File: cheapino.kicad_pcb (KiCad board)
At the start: 2 copper layers, 132.5 x 95.1 mm, 52 parts, among them K1 SW_Push, K10 SW_Push, K11 SW_Push, K12 SW_Push, K13 SW_Push, K14 SW_Push, K15 SW_Push, K16 SW_Push, K17 SW_Push, K18 SW_Push, K2 SW_Push, K3 SW_Push, K4 SW_Push, K5 SW_Push, K6 SW_Push, K7 SW_Push, K8 SW_Push, K9 SW_Push, U1 RP2040-Zero

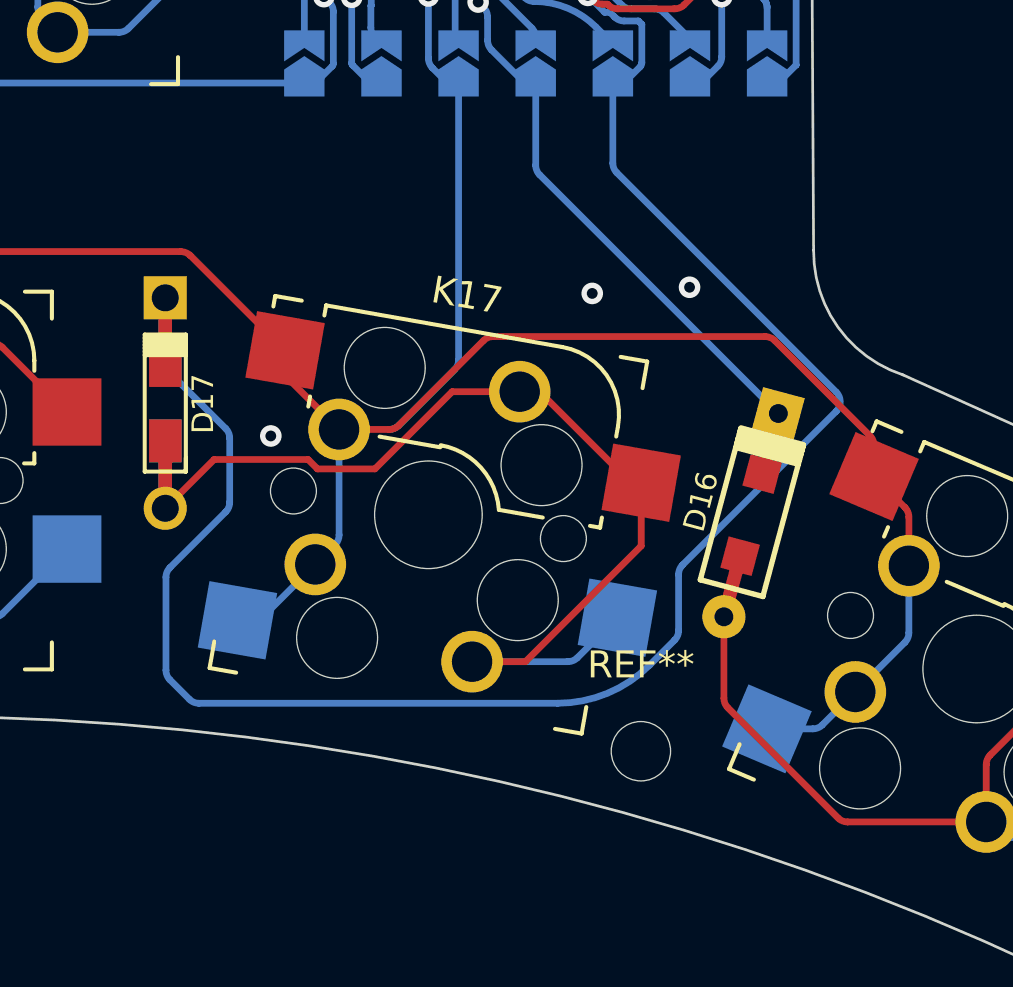
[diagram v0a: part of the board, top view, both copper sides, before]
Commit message: Fix missing SMD footprint on right/back Diodo D16
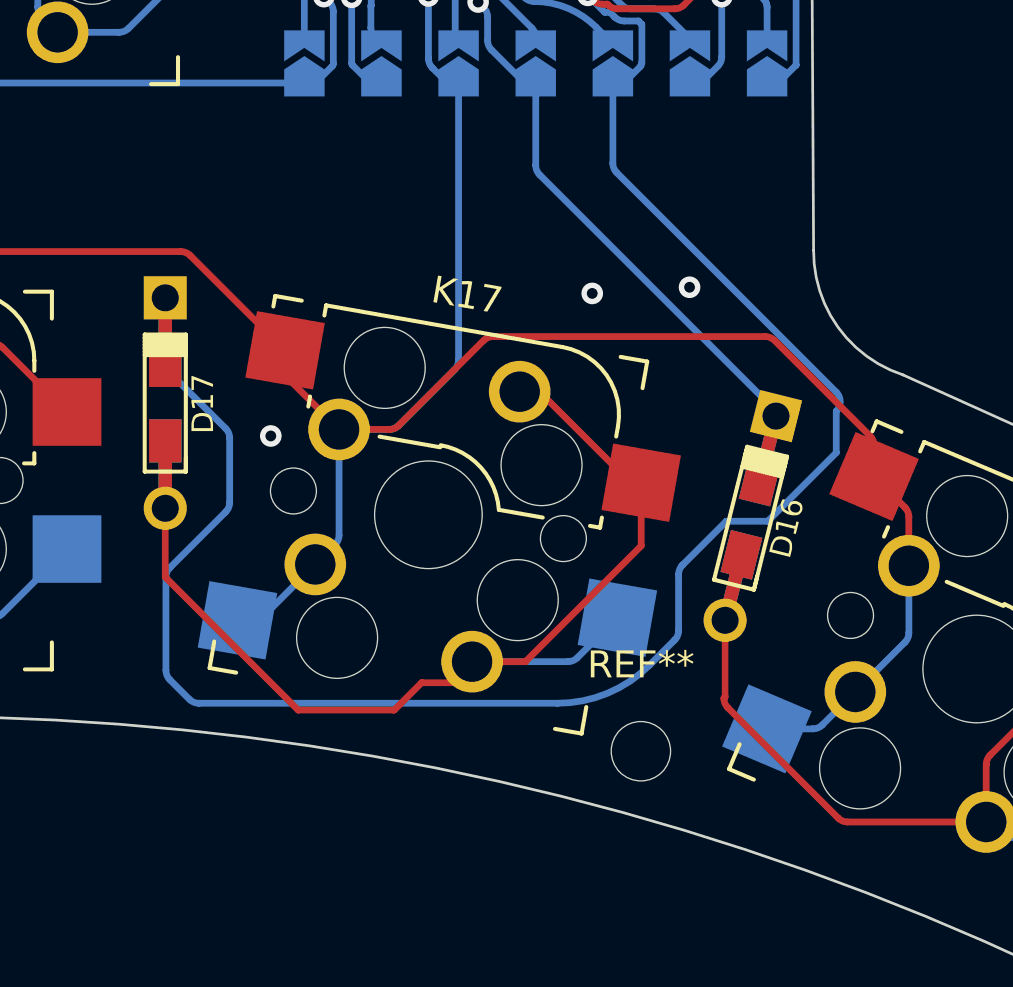
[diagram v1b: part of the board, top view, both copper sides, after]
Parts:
- D16: footprint keyboard_parts:D_SOD123_axial -> keebio:Diode-dual
- moved D16 0.12 mm to (173.2, 124.0), turned to 76 degrees
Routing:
- net Net-(D17-A): track 36.4 -> 37.9 mm
- net ROW_2: track 207.0 -> 207.9 mm

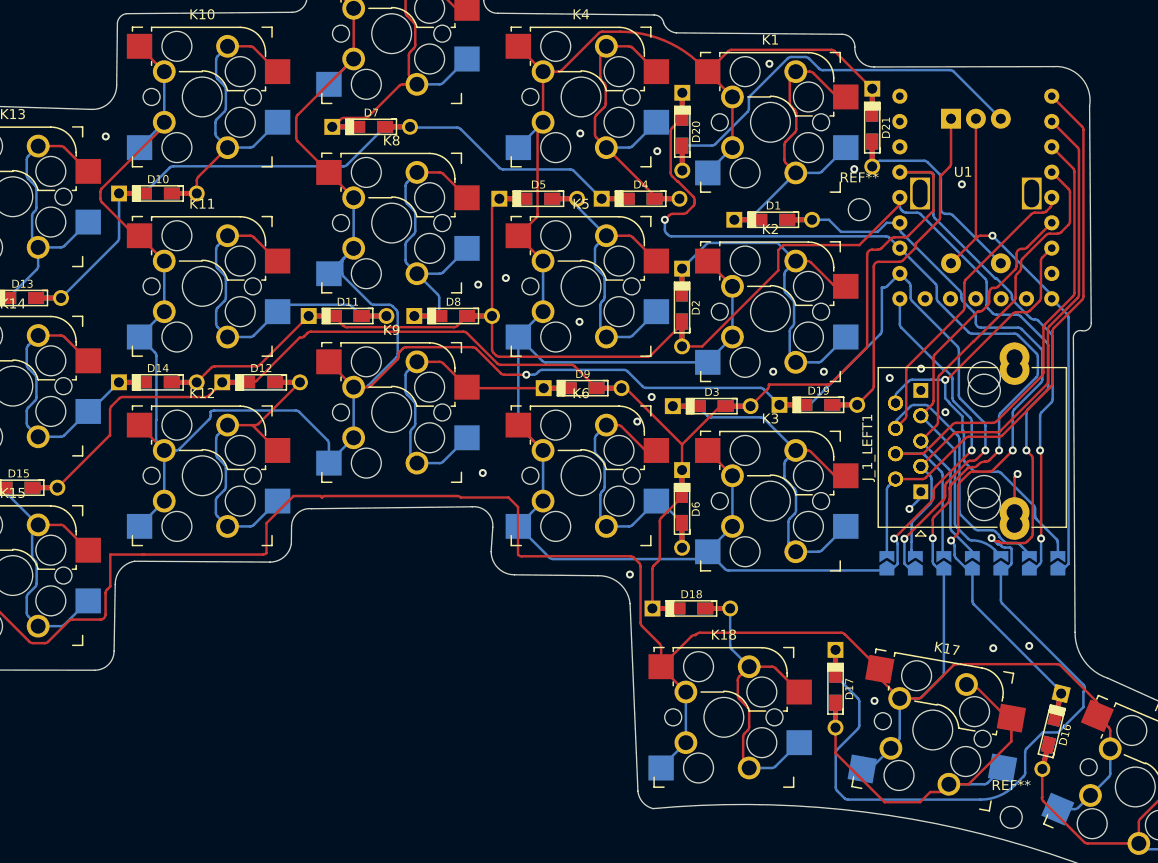
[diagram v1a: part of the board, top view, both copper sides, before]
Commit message: Fixes #10 Added some mounting holes
Also added logo, rounded tracks and tear drops
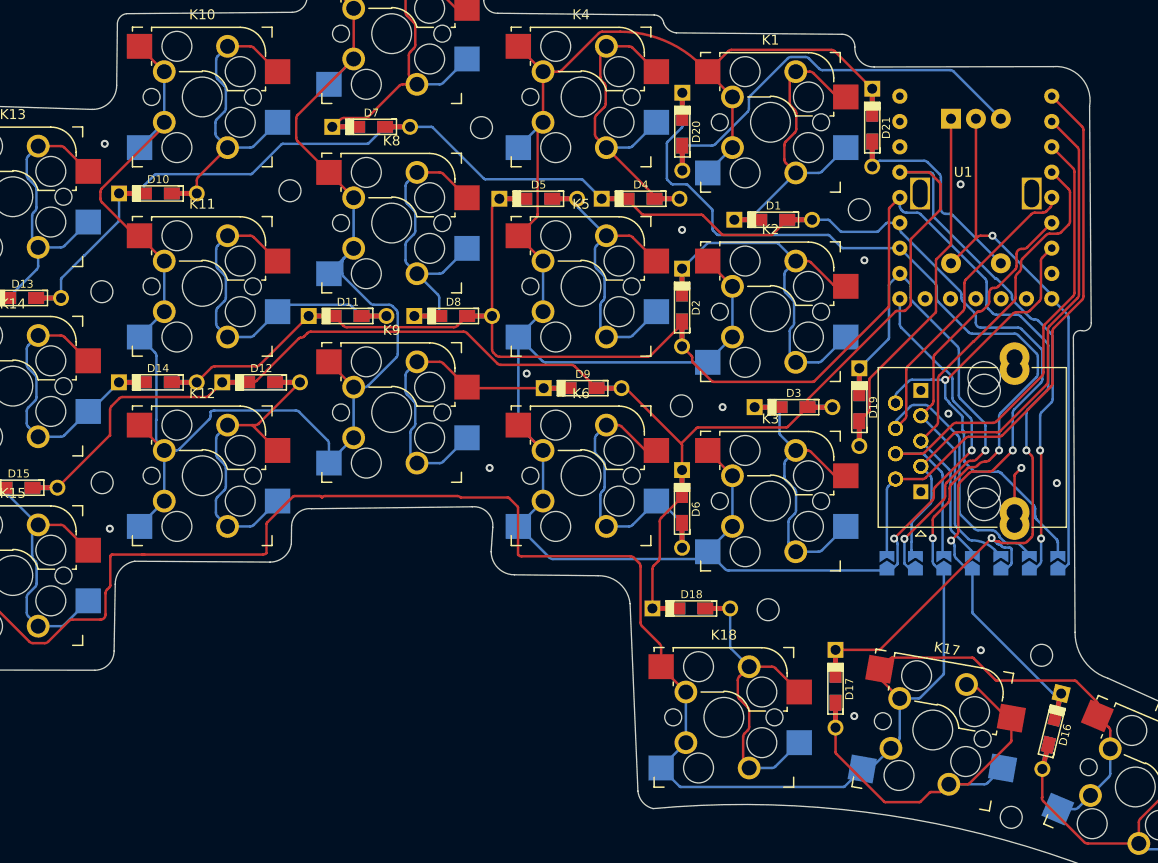
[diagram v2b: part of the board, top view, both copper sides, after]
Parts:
- added REF**: MountingHole_2.2mm_M2, MountingHole:MountingHole_2.2mm_M2, F.Cu at (136.1, 91.3)
- added REF**: MountingHole_2.2mm_M2, MountingHole:MountingHole_2.2mm_M2, F.Cu at (144.8, 111.8)
- added REF**: MountingHole_2.2mm_M2, MountingHole:MountingHole_2.2mm_M2, F.Cu at (78.0, 99.0)
- added REF**: MountingHole_2.2mm_M2, MountingHole:MountingHole_2.2mm_M2, F.Cu at (116.0, 63.4)
- added REF**: MountingHole_2.2mm_M2, MountingHole:MountingHole_2.2mm_M2, F.Cu at (96.8, 69.7)
- added REF**: MountingHole_2.2mm_M2, MountingHole:MountingHole_2.2mm_M2, F.Cu at (77.9, 79.9)
- added REF**: MountingHole_2.2mm_M2, MountingHole:MountingHole_2.2mm_M2, F.Cu at (172.2, 116.3)
- moved D3 8.20 mm to (147.3, 91.4)
- moved D19 4.12 mm to (153.9, 91.4), turned to 90 degrees
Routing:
- net COL_2: track 259.3 -> 205.7 mm, vias 3 -> 2
- net ROW_2: track 207.9 -> 174.8 mm
- net ROW_1: track 138.6 -> 155.4 mm
- net COL_3: track 343.4 -> 336.5 mm, vias 3 -> 2
- net Net-(D3-K): track 35.3 -> 28.7 mm
- net ROW_3: track 178.4 -> 181.0 mm
- net GND: track 8.88 -> 7.26 mm, vias 23 -> 13
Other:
- board text added: "Cheapino 2"
- board text added: "Solder on right side only"
- board text added: "by Tompi"
- board text removed: "Cheapino v2"
- board text removed: "Solder right side only"

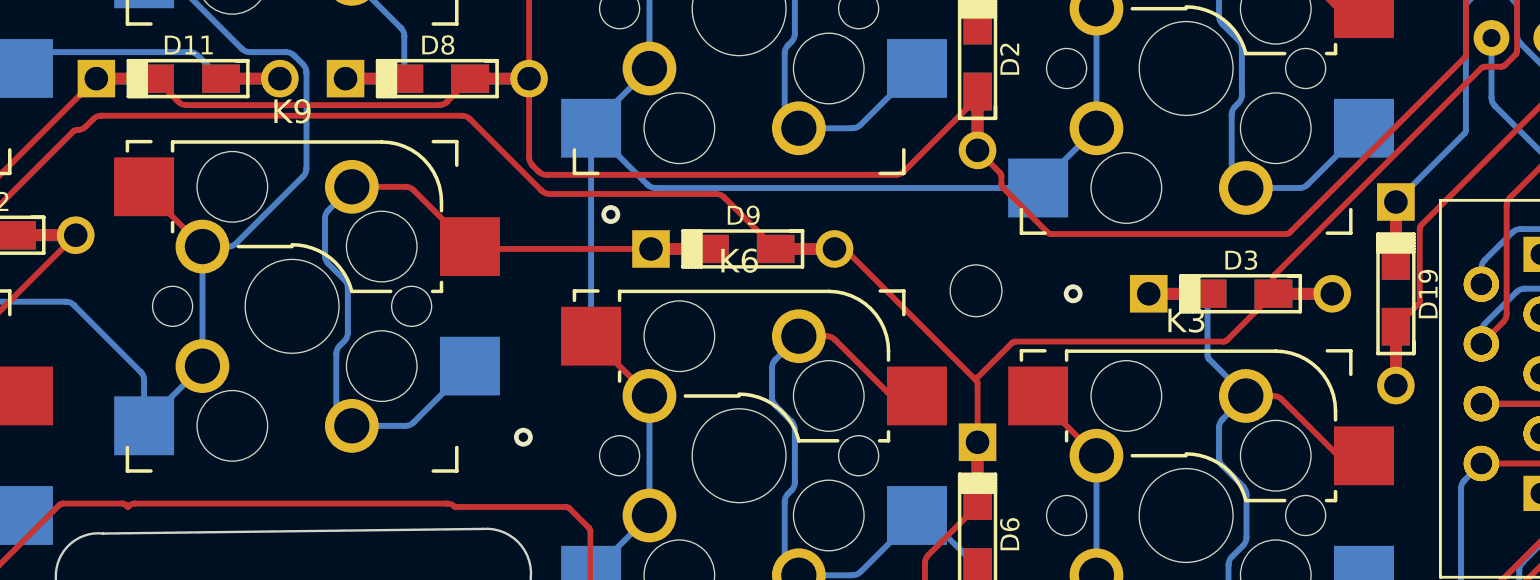
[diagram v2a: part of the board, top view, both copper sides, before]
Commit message: Fix embarassing missing trace for column 2...
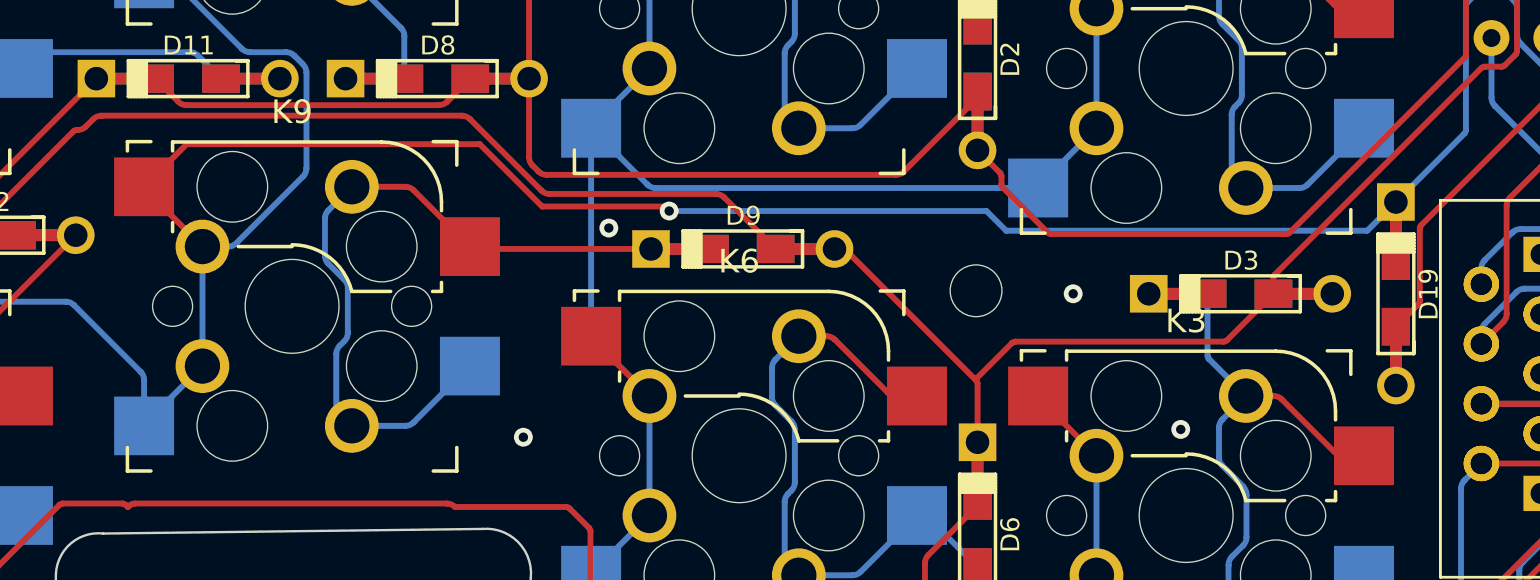
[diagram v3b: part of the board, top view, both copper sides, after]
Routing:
- net COL_2: track 205.7 -> 261.6 mm, vias 2 -> 3
- net GND: vias 13 -> 14
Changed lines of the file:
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@@
   (gr_text "Cheapino 2" (at 174.001658 114.960259) (layer "B.Paste")
     (effects (font (face "Impact") (size 4 4) (thickness 0.15)) (justify left bottom mirror))
-    (render_cache "Cheapino 2" -0
+    (render_cache "Cheapino 2" 0
       (polygon
         (pts
@@
   (segment (start 103.2002 51.435) (end 103.2002 56.515) (width 0.25) (layer "F.Cu") (net 23))
   (segment (start 165.678247 96.678353) (end 166.5732 95.7834) (width 0.25) (layer "F.Cu") (net 23))
+  (segment (start 114.985748 85.0784) (end 117.638948 87.7316) (width 0.25) (layer "F.Cu") (net 23))
   (segment (start 100.7202 86.9534) (end 103.2002 89.4334) (width 0.25) (layer "F.Cu") (net 23))
+  (segment (start 102.5352 85.0784) (end 114.985748 85.0784) (width 0.25) (layer "F.Cu") (net 23))
   (segment (start 77.8002 70.531893) (end 77.8002 69.846507) (width 0.25) (layer "F.Cu") (net 23))
   (segment (start 100.7202 67.8942) (end 100.7202 67.9542) (width 0.25) (layer "F.Cu") (net 23))
@@
   (segment (start 81.721 93.3034) (end 84.201 95.7834) (width 0.25) (layer "F.Cu") (net 23))
   (segment (start 97.585047 62.130153) (end 103.2002 56.515) (width 0.25) (layer "F.Cu") (net 23))
+  (segment (start 117.638948 87.7316) (end 122.8465 87.7316) (width 0.25) (layer "F.Cu") (net 23))
   (segment (start 81.721 74.3042) (end 84.201 76.7842) (width 0.25) (layer "F.Cu") (net 23))
   (segment (start 162.681047 99.015153) (end 164.724954 96.971246) (width 0.25) (layer "F.Cu") (net 23))
+  (segment (start 122.8465 87.7316) (end 123.0376 87.9227) (width 0.25) (layer "F.Cu") (net 23))
   (segment (start 158.4452 104.648) (end 162.388154 100.705046) (width 0.25) (layer "F.Cu") (net 23))
+  (segment (start 100.7202 86.8934) (end 102.5352 85.0784) (width 0.25) (layer "F.Cu") (net 23))
   (segment (start 81.3054 74.2442) (end 77.946646 70.885446) (width 0.25) (layer "F.Cu") (net 23))
   (segment (start 162.5346 100.351493) (end 162.5346 99.368707) (width 0.25) (layer "F.Cu") (net 23))
@@
   (via (at 166.5732 95.7834) (size 0.8) (drill 0.4) (layers "F.Cu" "B.Cu") (free) (net 23))
   (via (at 158.4452 104.648) (size 0.8) (drill 0.4) (layers "F.Cu" "B.Cu") (free) (net 23))
+  (via (at 123.0376 87.9227) (size 0.8) (drill 0.4) (layers "F.Cu" "B.Cu") (free) (net 23))
   (arc (start 162.681047 99.015153) (mid 162.57266 99.177365) (end 162.5346 99.368707) (width 0.25) (layer "F.Cu") (net 23))
   (arc (start 162.388154 100.705046) (mid 162.49654 100.542834) (end 162.5346 100.351493) (width 0.25) (layer "F.Cu") (net 23))
@@
   (segment (start 83.4136 92.71) (end 83.3882 92.7354) (width 0.25) (layer "B.Cu") (net 23))
   (segment (start 83.4136 86.303907) (end 83.4136 92.71) (width 0.25) (layer "B.Cu") (net 23))
+  (segment (start 123.0376 87.9227) (end 136.5221 87.9227) (width 0.25) (layer "B.Cu") (net 23))
   (segment (start 81.721 84.4042) (end 83.267154 85.950354) (width 0.25) (layer "B.Cu") (net 23))
   (segment (start 100.573753 94.757153) (end 97.738446 91.921846) (width 0.25) (layer "B.Cu") (net 23))
   (segment (start 83.534647 95.117047) (end 84.201 95.7834) (width 0.25) (layer "B.Cu") (net 23))
   (segment (start 102.203647 78.354445) (end 104.873756 81.024554) (width 0.25) (layer "B.Cu") (net 23))
+  (segment (start 137.3586 88.7592) (end 152.7048 88.7592) (width 0.25) (layer "B.Cu") (net 23))
   (segment (start 163.9062 90.242293) (end 163.9062 85.691358) (width 0.25) (layer "B.Cu") (net 23))
+  (segment (start 136.5221 87.9227) (end 137.3586 88.7592) (width 0.25) (layer "B.Cu") (net 23))
   (segment (start 84.201 76.7842) (end 84.201 81.8642) (width 0.25) (layer "B.Cu") (net 23))
   (segment (start 88.849953 91.921847) (end 88.8492 91.9226) (width 0.25) (layer "B.Cu") (net 23))
@@
   (segment (start 100.7202 97.0534) (end 100.7202 95.110707) (width 0.25) (layer "B.Cu") (net 23))
   (segment (start 84.201 57.785) (end 84.201 62.865) (width 0.25) (layer "B.Cu") (net 23))
+  (segment (start 152.7048 88.7592) (end 153.924 87.54) (width 0.25) (layer "B.Cu") (net 23))
   (segment (start 163.759753 85.337804) (end 159.221446 80.799497) (width 0.25) (layer "B.Cu") (net 23))
   (segment (start 97.384893 91.7754) (end 89.203507 91.7754) (width 0.25) (layer "B.Cu") (net 23))
@@
   (via (at 153.416 122.428) (size 0.8) (drill 0.4) (layers "F.Cu" "B.Cu") (free) (net 36))
   (via (at 173.736 99.06) (size 0.8) (drill 0.4) (layers "F.Cu" "B.Cu") (free) (net 36))
-  (via (at 120.556992 88.071523) (size 0.8) (drill 0.4) (layers "F.Cu" "B.Cu") (free) (net 36))
+  (via (at 120.4722 88.646) (size 0.8) (drill 0.4) (layers "F.Cu" "B.Cu") (free) (net 36))
   (via (at 170.18 97.536) (size 0.8) (drill 0.4) (layers "F.Cu" "B.Cu") (free) (net 36))
   (via (at 78.74 103.632) (size 0.8) (drill 0.4) (layers "F.Cu" "B.Cu") (free) (net 36))
@@
   (via (at 116.84 97.536) (size 0.8) (drill 0.4) (layers "F.Cu" "B.Cu") (free) (net 36))
   (via (at 154.432 76.708) (size 0.8) (drill 0.4) (layers "F.Cu" "B.Cu") (free) (net 36))
+  (via (at 144.78 97.2058) (size 0.8) (drill 0.4) (layers "F.Cu" "B.Cu") (free) (net 36))
   (via (at 140.208 91.44) (size 0.8) (drill 0.4) (layers "F.Cu" "B.Cu") (free) (net 36))
   (arc (start 169.554779 98.161221) (mid 169.511424 98.226106) (end 169.4962 98.302643) (width 0.25) (layer "F.Cu") (net 36))
